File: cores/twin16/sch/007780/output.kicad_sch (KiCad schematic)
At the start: 97 parts, among them J2 FDR, J28 T34, K11 FDR, K48 X2B, K54 X2B

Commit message: twin16 - wip - sch labels
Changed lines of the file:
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@@
 	(bus
 		(pts
-			(xy 205.74 24.13) (xy 353.06 24.13)
-		)
-		(stroke
-			(width 0)
-			(type default)
-		)
-	)
-	(bus
-		(pts
 			(xy 55.88 182.88) (xy 55.88 185.42)
 		)
@@
 	(bus
 		(pts
-			(xy 71.12 266.7) (xy 69.85 266.7)
+			(xy 69.85 267.97) (xy 218.44 267.97)
 		)
 		(stroke
@@
 		)
 	)
-	(bus
-		(pts
-			(xy 218.44 267.97) (xy 71.12 267.97)
-		)
-		(stroke
-			(width 0)
-			(type default)
-		)
-	)
 	(wire
 		(pts
@@
 	(bus
 		(pts
-			(xy 205.74 25.4) (xy 204.47 25.4)
+			(xy 204.47 24.13) (xy 353.06 24.13)
 		)
 		(stroke
@@
 	(bus
 		(pts
-			(xy 71.12 267.97) (xy 71.12 266.7)
-		)
-		(stroke
-			(width 0)
-			(type default)
-		)
-	)
-	(bus
-		(pts
 			(xy 67.31 247.65) (xy 68.58 247.65)
 		)
@@
 		)
 	)
-	(bus
-		(pts
-			(xy 205.74 24.13) (xy 205.74 25.4)
-		)
-		(stroke
-			(width 0)
-			(type default)
-		)
-	)
 	(wire
 		(pts
@@
 	(bus
 		(pts
-			(xy 204.47 25.4) (xy 204.47 59.69)
+			(xy 204.47 24.13) (xy 204.47 59.69)
 		)
 		(stroke
@@
 	(bus
 		(pts
-			(xy 69.85 266.7) (xy 69.85 236.22)
+			(xy 69.85 267.97) (xy 69.85 236.22)
 		)
 		(stroke

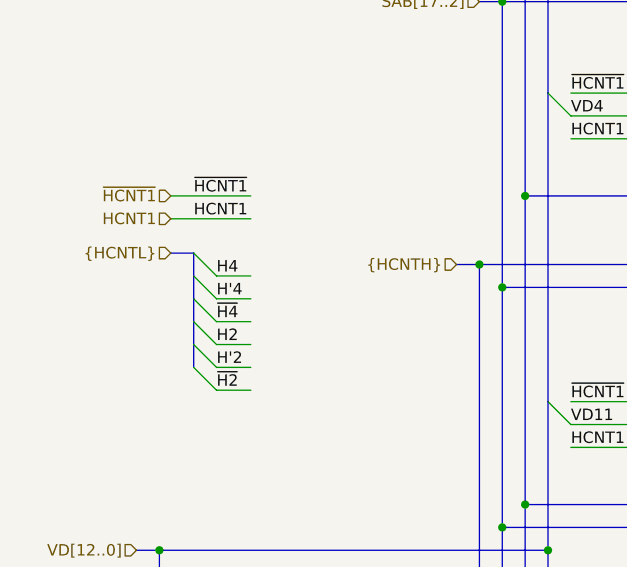
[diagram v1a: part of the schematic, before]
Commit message: twin16: boots up to RAM/ROM check screen
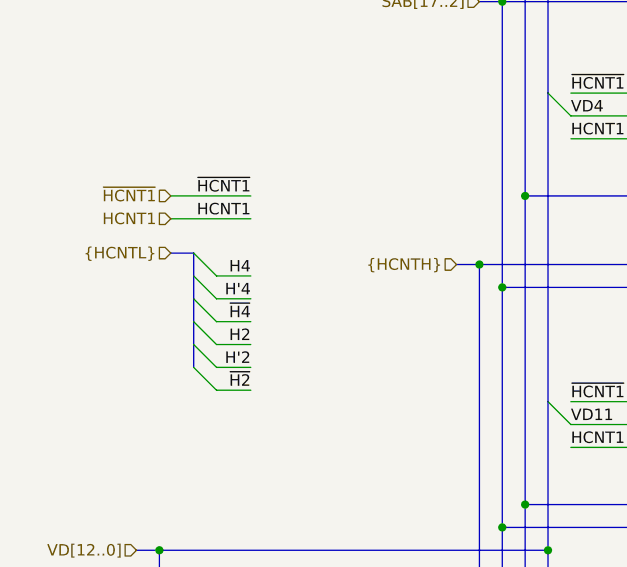
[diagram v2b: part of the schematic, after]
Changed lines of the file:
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@@
 	)
 	(label "H2"
-		(at 33.02 83.82 0)
-		(fields_autoplaced yes)
-		(effects
-			(font
-				(size 1.27 1.27)
-			)
-			(justify left bottom)
+		(at 36.83 83.82 180)
+		(fields_autoplaced yes)
+		(effects
+			(font
+				(size 1.27 1.27)
+			)
+			(justify right bottom)
 		)
 	)
@@
 	)
 	(label "~{H4}"
-		(at 33.02 81.28 0)
-		(fields_autoplaced yes)
-		(effects
-			(font
-				(size 1.27 1.27)
-			)
-			(justify left bottom)
+		(at 36.83 81.28 180)
+		(fields_autoplaced yes)
+		(effects
+			(font
+				(size 1.27 1.27)
+			)
+			(justify right bottom)
 		)
 	)
@@
 	)
 	(label "H'4"
-		(at 33.02 78.74 0)
-		(fields_autoplaced yes)
-		(effects
-			(font
-				(size 1.27 1.27)
-			)
-			(justify left bottom)
+		(at 36.83 78.74 180)
+		(fields_autoplaced yes)
+		(effects
+			(font
+				(size 1.27 1.27)
+			)
+			(justify right bottom)
 		)
 	)
@@
 	)
 	(label "H'2"
-		(at 33.02 86.36 0)
-		(fields_autoplaced yes)
-		(effects
-			(font
-				(size 1.27 1.27)
-			)
-			(justify left bottom)
+		(at 36.83 86.36 180)
+		(fields_autoplaced yes)
+		(effects
+			(font
+				(size 1.27 1.27)
+			)
+			(justify right bottom)
 		)
 	)
 	(label "~{HCNT1}"
-		(at 30.48 67.31 0)
-		(fields_autoplaced yes)
-		(effects
-			(font
-				(size 1.27 1.27)
-			)
-			(justify left bottom)
+		(at 36.83 67.31 180)
+		(fields_autoplaced yes)
+		(effects
+			(font
+				(size 1.27 1.27)
+			)
+			(justify right bottom)
 		)
 	)
@@
 	)
 	(label "~{H2}"
-		(at 33.02 88.9 0)
-		(fields_autoplaced yes)
-		(effects
-			(font
-				(size 1.27 1.27)
-			)
-			(justify left bottom)
+		(at 36.83 88.9 180)
+		(fields_autoplaced yes)
+		(effects
+			(font
+				(size 1.27 1.27)
+			)
+			(justify right bottom)
 		)
 	)
@@
 	)
 	(label "H4"
-		(at 33.02 76.2 0)
-		(fields_autoplaced yes)
-		(effects
-			(font
-				(size 1.27 1.27)
-			)
-			(justify left bottom)
+		(at 36.83 76.2 180)
+		(fields_autoplaced yes)
+		(effects
+			(font
+				(size 1.27 1.27)
+			)
+			(justify right bottom)
 		)
 	)
@@
 	)
 	(label "HCNT1"
-		(at 30.48 69.85 0)
-		(fields_autoplaced yes)
-		(effects
-			(font
-				(size 1.27 1.27)
-			)
-			(justify left bottom)
-		)
-	)
+		(at 36.83 69.85 180)
+		(fields_autoplaced yes)
+		(effects
+			(font
+				(size 1.27 1.27)
+			)
+			(justify right bottom)
+		)
+	)
